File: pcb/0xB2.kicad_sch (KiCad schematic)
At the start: 37 parts, among them J1 USB_C_Receptacle_USB2.0, J2 Conn_01x12, J3 Conn_01x05, J4 Conn_01x12, SW1 SW_Push, SW2 SW_Push, U1 RP2040, U2 W25Q32JVZP, U3 AP2127K-3.3, Y1 Crystal_GND24

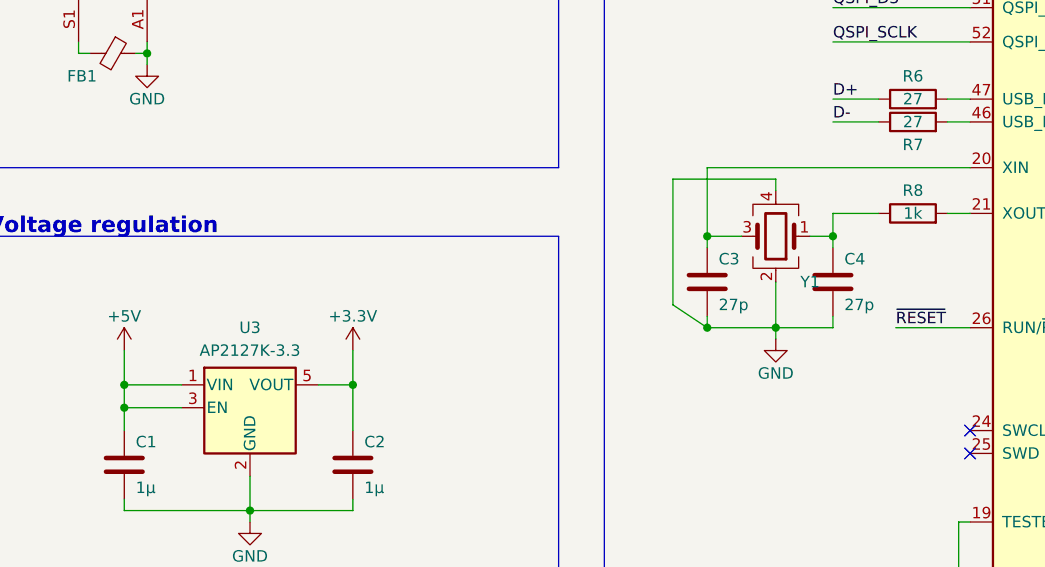
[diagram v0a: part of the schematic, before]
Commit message: Smaller crystal footprint > 2520
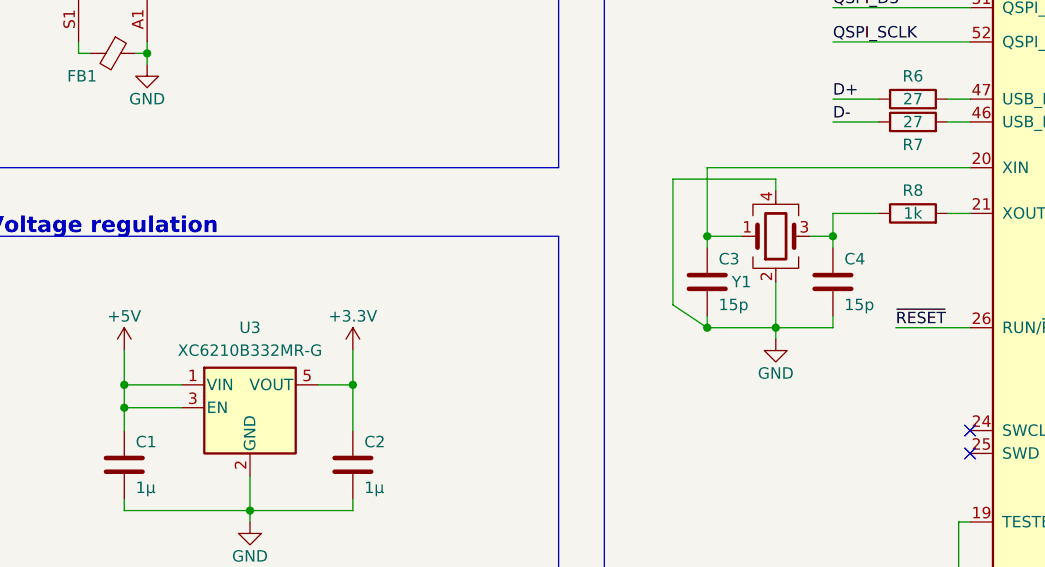
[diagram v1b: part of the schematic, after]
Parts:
- C3, C4: value 27p -> 15p; LCSC C1557 -> C1548
- U3: value AP2127K-3.3 -> XC6210B332MR-G; LCSC C47719 -> C82942; LCSC2 (none) -> C47719
- Y1: footprint Crystal:Crystal_SMD_3225-4Pin_3.2x2.5mm -> Crystal:Crystal_SMD_2520-4Pin_2.5x2.0mm; LCSC C97242 -> C2149204
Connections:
- net at C3.1, U1.20 (XIN): now also Y1.1; no longer Y1.3
- net at C4.1, R8.1: now also Y1.3; no longer Y1.1
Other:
- moved on the sheet: Y1
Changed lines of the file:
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@@
     (in_bom yes) (on_board yes)
     (property "Reference" "U3" (id 0) (at 46.99 106.68 0))
-    (property "Value" "AP2127K-3.3" (id 1) (at 46.99 109.22 0))
+    (property "Value" "XC6210B332MR-G" (id 1) (at 46.99 109.22 0))
     (property "Footprint" "Package_TO_SOT_SMD:SOT-23-5" (id 2) (at 46.99 107.315 0)
       (effects (font (size 1.27 1.27)) hide)
     )
-    (property "Datasheet" "https://www.diodes.com/assets/Datasheets/AP2127.pdf" (id 3) (at 46.99 113.03 0)
-      (effects (font (size 1.27 1.27)) hide)
-    )
-    (property "LCSC" "C47719" (id 4) (at 46.99 115.57 0)
+    (property "Datasheet" "" (id 3) (at 46.99 113.03 0)
+      (effects (font (size 1.27 1.27)) hide)
+    )
+    (property "LCSC" "C82942" (id 4) (at 46.99 115.57 0)
+      (effects (font (size 1.27 1.27)) hide)
+    )
+    (property "LCSC2" "C47719" (id 5) (at 46.99 115.57 0)
       (effects (font (size 1.27 1.27)) hide)
     )
@@
     (pin "2")
   )
-  (symbol (lib_id "Device:Crystal_GND24") (at 105.41 96.52 180) (unit 1)
-    (in_bom yes) (on_board yes)
-    (property "Reference" "Y1" (id 0) (at 109.22 101.6 0))
-    (property "Value" "Crystal_GND24" (id 1) (at 93.98 97.5614 0)
-      (effects (font (size 1.27 1.27)) hide)
-    )
-    (property "Footprint" "Crystal:Crystal_SMD_3225-4Pin_3.2x2.5mm" (id 2) (at 105.41 96.52 0)
+  (symbol (lib_id "Device:Crystal_GND24") (at 105.41 96.52 0) (mirror x) (unit 1)
+    (in_bom yes) (on_board yes)
+    (property "Reference" "Y1" (id 0) (at 101.6 101.6 0))
+    (property "Value" "Crystal_GND24" (id 1) (at 116.84 97.5614 0)
+      (effects (font (size 1.27 1.27)) hide)
+    )
+    (property "Footprint" "Crystal:Crystal_SMD_2520-4Pin_2.5x2.0mm" (id 2) (at 105.41 96.52 0)
       (effects (font (size 1.27 1.27)) hide)
     )
@@
       (effects (font (size 1.27 1.27)) hide)
     )
-    (property "LCSC" "C97242" (id 4) (at 105.41 96.52 0)
+    (property "LCSC" "C2149204" (id 4) (at 105.41 96.52 0)
       (effects (font (size 1.27 1.27)) hide)
     )
@@
       (effects (font (size 1.27 1.27)) (justify left))
     )
-    (property "Value" "27p" (id 1) (at 113.03 104.14 0)
+    (property "Value" "15p" (id 1) (at 113.03 104.14 0)
       (effects (font (size 1.27 1.27)) (justify left))
     )
@@
       (effects (font (size 1.27 1.27)) hide)
     )
-    (property "LCSC" "C1557" (id 4) (at 111.76 101.6 0)
+    (property "LCSC" "C1548" (id 4) (at 111.76 101.6 0)
       (effects (font (size 1.27 1.27)) hide)
     )
@@
       (effects (font (size 1.27 1.27)) (justify left))
     )
-    (property "Value" "27p" (id 1) (at 99.06 104.14 0)
+    (property "Value" "15p" (id 1) (at 99.06 104.14 0)
       (effects (font (size 1.27 1.27)) (justify left))
     )
@@
       (effects (font (size 1.27 1.27)) hide)
     )
-    (property "LCSC" "C1557" (id 4) (at 97.79 101.6 0)
+    (property "LCSC" "C1548" (id 4) (at 97.79 101.6 0)
       (effects (font (size 1.27 1.27)) hide)
     )
@@
     )
     (path "/c0b12aba-3c4f-4684-83d7-a5de2c7f97e9"
-      (reference "C3") (unit 1) (value "27p") (footprint "Capacitor_SMD:C_0402_1005Metric")
+      (reference "C3") (unit 1) (value "15p") (footprint "Capacitor_SMD:C_0402_1005Metric")
     )
     (path "/89a664f3-9470-4cc9-8840-97b4b2b29405"
-      (reference "C4") (unit 1) (value "27p") (footprint "Capacitor_SMD:C_0402_1005Metric")
+      (reference "C4") (unit 1) (value "15p") (footprint "Capacitor_SMD:C_0402_1005Metric")
     )
     (path "/3ed857fe-184a-43ae-8f36-82703b1b8349"
@@
     )
     (path "/33208a57-5054-4bad-b85f-35da7b25e7bb"
-      (reference "U3") (unit 1) (value "AP2127K-3.3") (footprint "Package_TO_SOT_SMD:SOT-23-5")
+      (reference "U3") (unit 1) (value "XC6210B332MR-G") (footprint "Package_TO_SOT_SMD:SOT-23-5")
     )
     (path "/4ba8f30d-b9de-4dee-94c4-5459f9c13a42"
-      (reference "Y1") (unit 1) (value "Crystal_GND24") (footprint "Crystal:Crystal_SMD_3225-4Pin_3.2x2.5mm")
-    )
-  )
+      (reference "Y1") (unit 1) (value "Crystal_GND24") (footprint "Crystal:Crystal_SMD_2520-4Pin_2.5x2.0mm")
+    )
+  )

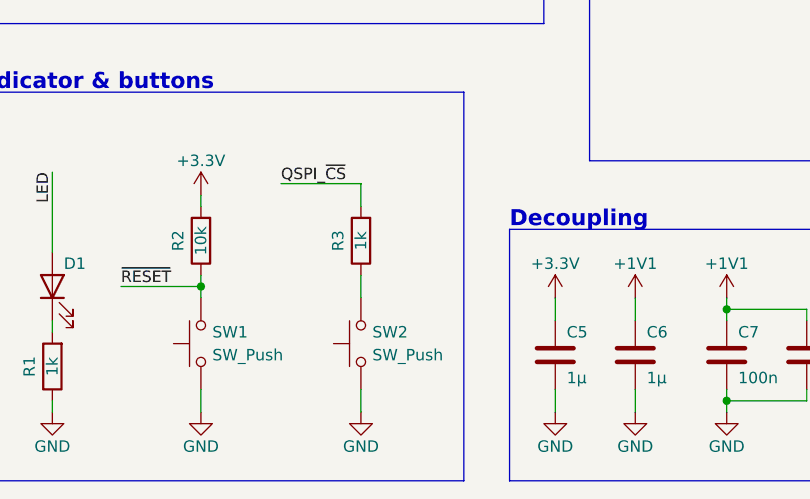
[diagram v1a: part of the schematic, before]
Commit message: Add BOOT pad on bottom layer
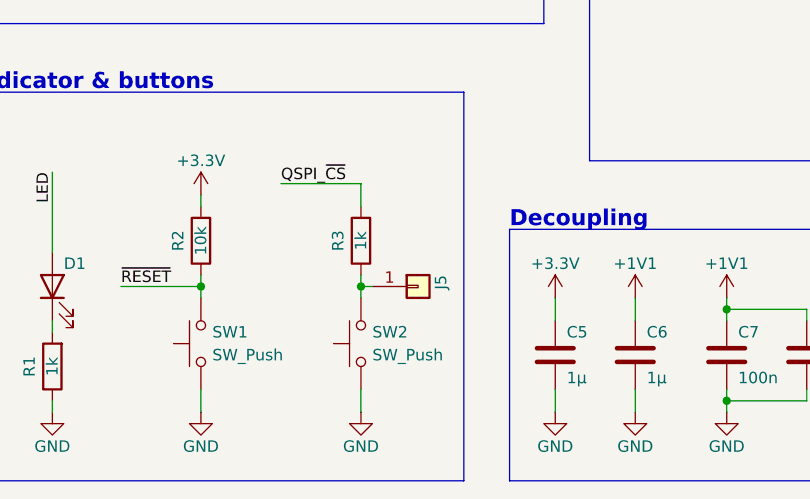
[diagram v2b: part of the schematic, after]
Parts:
- added J5: Conn_01x01, TestPoint:TestPoint_Pad_D1.0mm, symbol Connector_Generic:Conn_01x01
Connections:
- net at R3.1, SW2.2: now also J5.1 (Pin_1)
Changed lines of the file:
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@@
   (junction (at 71.12 44.45) (diameter 0) (color 0 0 0 0)
+  )
+  (junction (at 60.96 172.72) (diameter 0) (color 0 0 0 0)
   )
   (junction (at 130.81 185.42) (diameter 0) (color 0 0 0 0)
@@
     (stroke (width 0) (type default) (color 0 0 0 0))
   )
-  (wire (pts (xy 60.96 171.45) (xy 60.96 173.99))
+  (wire (pts (xy 60.96 171.45) (xy 60.96 172.72))
     (stroke (width 0) (type default) (color 0 0 0 0))
   )
@@
     (stroke (width 0) (type default) (color 0 0 0 0))
   )
+  (wire (pts (xy 60.96 172.72) (xy 60.96 173.99))
+    (stroke (width 0) (type default) (color 0 0 0 0))
+  )
   (wire (pts (xy 228.6 64.77) (xy 237.49 64.77))
     (stroke (width 0) (type default) (color 0 0 0 0))
@@
   )
   (wire (pts (xy 165.1 40.64) (xy 165.1 38.1))
+    (stroke (width 0) (type default) (color 0 0 0 0))
+  )
+  (wire (pts (xy 60.96 172.72) (xy 62.23 172.72))
     (stroke (width 0) (type default) (color 0 0 0 0))
   )
@@
     (pin "1")
   )
+  (symbol (lib_id "Connector_Generic:Conn_01x01") (at 67.31 172.72 0) (unit 1)
+    (in_bom yes) (on_board yes)
+    (property "Reference" "J5" (id 0) (at 69.85 171.45 90)
+      (effects (font (size 1.27 1.27)) (justify right))
+    )
+    (property "Value" "Conn_01x01" (id 1) (at 66.0401 175.26 90)
+      (effects (font (size 1.27 1.27)) (justify right) hide)
+    )
+    (property "Footprint" "TestPoint:TestPoint_Pad_D1.0mm" (id 2) (at 67.31 172.72 0)
+      (effects (font (size 1.27 1.27)) hide)
+    )
+    (property "Datasheet" "~" (id 3) (at 67.31 172.72 0)
+      (effects (font (size 1.27 1.27)) hide)
+    )
+    (pin "1")
+  )
   (symbol (lib_id "power:GND") (at 261.62 69.215 0) (unit 1)
     (in_bom yes) (on_board yes)
@@
       (reference "J4") (unit 1) (value "Conn_01x12") (footprint "0xLib_Connectors:PinHeader_1x12_P2.54mm")
     )
+    (path "/bc3a4b7a-f2c8-40bd-ac75-89d3e5ce5d5b"
+      (reference "J5") (unit 1) (value "Conn_01x01") (footprint "TestPoint:TestPoint_Pad_D1.0mm")
+    )
     (path "/81213cff-519c-4fcf-ae25-6fad0fc859bb"

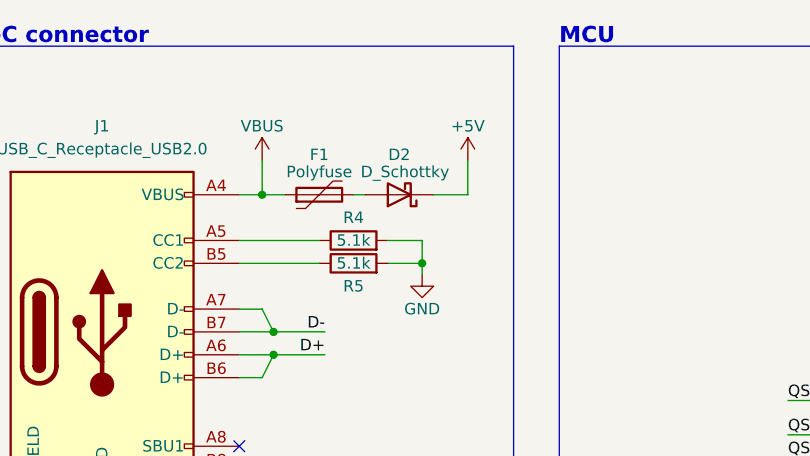
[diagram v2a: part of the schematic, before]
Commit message: New ref for D2
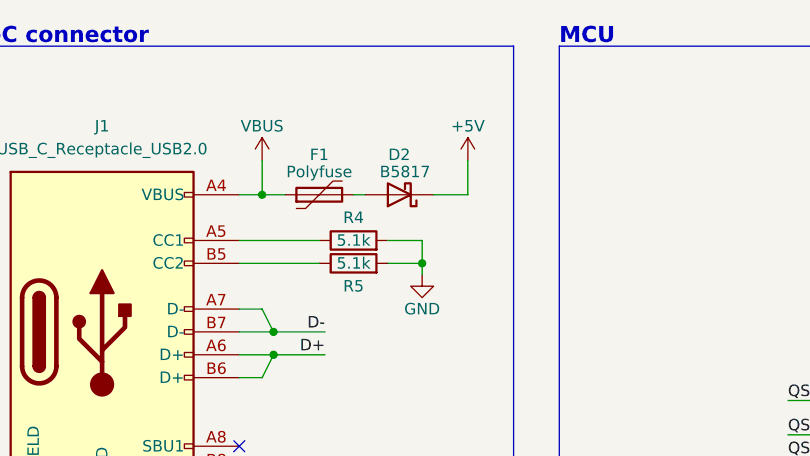
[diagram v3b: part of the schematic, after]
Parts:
- D2: value D_Schottky -> B5817; LCSC C22638 -> C123899
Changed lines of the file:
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@@
     (in_bom yes) (on_board yes)
     (property "Reference" "D2" (id 0) (at 68.58 32.385 0))
-    (property "Value" "D_Schottky" (id 1) (at 69.215 34.29 0))
+    (property "Value" "B5817" (id 1) (at 69.215 34.29 0))
     (property "Footprint" "Diode_SMD:D_SOD-323" (id 2) (at 68.58 36.83 0)
       (effects (font (size 1.27 1.27)) hide)
@@
       (effects (font (size 1.27 1.27)) hide)
     )
-    (property "LCSC" "C22638" (id 4) (at 68.58 36.83 0)
+    (property "LCSC" "C123899" (id 4) (at 68.58 36.83 0)
       (effects (font (size 1.27 1.27)) hide)
     )
@@
     )
     (path "/f97de4cd-aa39-42c5-ace3-9184b5a62b38"
-      (reference "D2") (unit 1) (value "D_Schottky") (footprint "Diode_SMD:D_SOD-323")
+      (reference "D2") (unit 1) (value "B5817") (footprint "Diode_SMD:D_SOD-323")
     )
     (path "/ce9365fe-085a-4731-86d8-fc3e6b16f716"

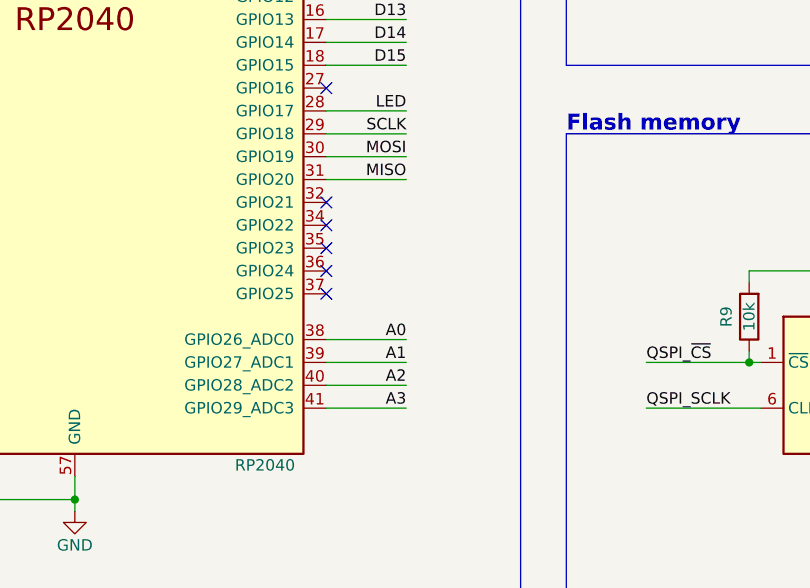
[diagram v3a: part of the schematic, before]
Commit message: Add USB VBUS detect on GPIO 25
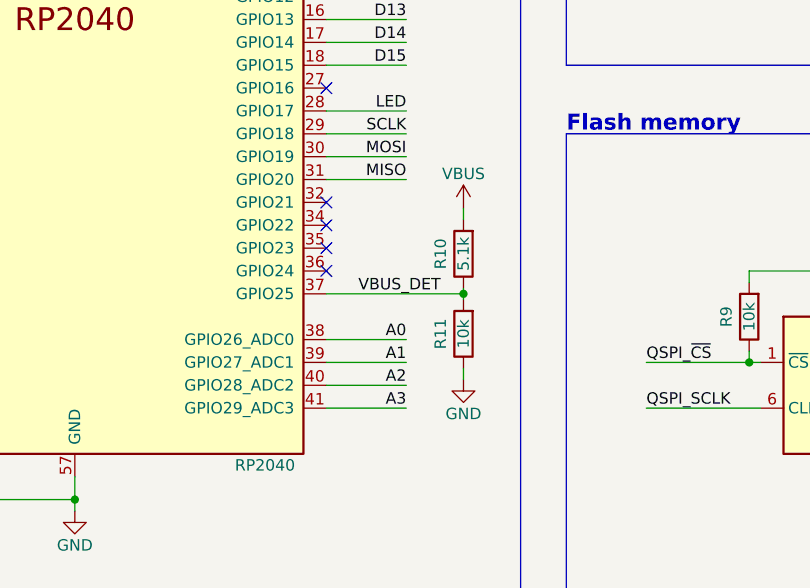
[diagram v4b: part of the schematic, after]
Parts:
- added R10: 5.1k, Resistor_SMD:R_0402_1005Metric, symbol Device:R
- added R11: 10k, Resistor_SMD:R_0402_1005Metric, symbol Device:R
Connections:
- net GND: now also R11.1
- net VBUS: now also R10.2
- net VBUS_DET: now reaches U1.37 (GPIO25)
- net VBUS_DET: now also R10.1, R11.2
- no-connect marks 10 -> 9
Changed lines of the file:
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@@
   (junction (at 35.56 76.2) (diameter 0) (color 0 0 0 0)
   )
+  (junction (at 198.12 121.92) (diameter 0) (color 0 0 0 0)
+  )
   (junction (at 231.14 46.99) (diameter 0) (color 0 0 0 0)
   )
@@
   )
   (no_connect (at 182.88 119.38))
-  (no_connect (at 182.88 121.92))
   (no_connect (at 182.88 116.84))
   (no_connect (at 182.88 111.76))
@@
     (stroke (width 0) (type default) (color 0 0 0 0))
   )
+  (wire (pts (xy 198.12 130.175) (xy 198.12 131.445))
+    (stroke (width 0) (type default) (color 0 0 0 0))
+  )
   (wire (pts (xy 143.51 38.1) (xy 143.51 40.64))
     (stroke (width 0) (type default) (color 0 0 0 0))
@@
     (stroke (width 0) (type default) (color 0 0 0 0))
   )
+  (wire (pts (xy 198.12 121.92) (xy 198.12 122.555))
+    (stroke (width 0) (type default) (color 0 0 0 0))
+  )
   (wire (pts (xy 139.7 184.15) (xy 139.7 185.42))
     (stroke (width 0) (type default) (color 0 0 0 0))
@@
     (stroke (width 0) (type default) (color 0 0 0 0))
   )
+  (wire (pts (xy 182.88 121.92) (xy 198.12 121.92))
+    (stroke (width 0) (type default) (color 0 0 0 0))
+  )
   (wire (pts (xy 243.84 119.38) (xy 243.84 121.92))
     (stroke (width 0) (type default) (color 0 0 0 0))
@@
     (stroke (width 0) (type default) (color 0 0 0 0))
   )
+  (wire (pts (xy 198.12 112.395) (xy 198.12 113.665))
+    (stroke (width 0) (type default) (color 0 0 0 0))
+  )
   (wire (pts (xy 124.46 83.82) (xy 127 83.82))
     (stroke (width 0) (type default) (color 0 0 0 0))
@@
   )
   (wire (pts (xy 162.56 38.1) (xy 162.56 40.64))
+    (stroke (width 0) (type default) (color 0 0 0 0))
+  )
+  (wire (pts (xy 198.12 121.285) (xy 198.12 121.92))
     (stroke (width 0) (type default) (color 0 0 0 0))
   )
@@
   )
   (label "D0" (at 237.49 39.37 180)
+    (effects (font (size 1.27 1.27)) (justify right bottom))
+  )
+  (label "VBUS_DET" (at 195.58 121.92 180)
     (effects (font (size 1.27 1.27)) (justify right bottom))
   )
@@
     (pin "2")
   )
+  (symbol (lib_id "Device:R") (at 198.12 117.475 180) (unit 1)
+    (in_bom yes) (on_board yes)
+    (property "Reference" "R10" (id 0) (at 195.58 117.475 90))
+    (property "Value" "5.1k" (id 1) (at 198.12 117.475 90))
+    (property "Footprint" "Resistor_SMD:R_0402_1005Metric" (id 2) (at 199.898 117.475 90)
+      (effects (font (size 1.27 1.27)) hide)
+    )
+    (property "Datasheet" "~" (id 3) (at 198.12 117.475 0)
+      (effects (font (size 1.27 1.27)) hide)
+    )
+    (property "LCSC" "C25905" (id 4) (at 198.12 117.475 0)
+      (effects (font (size 1.27 1.27)) hide)
+    )
+    (pin "1")
+    (pin "2")
+  )
   (symbol (lib_id "Device:C") (at 157.48 180.34 0) (unit 1)
     (in_bom yes) (on_board yes)
@@
     )
     (pin "1")
+  )
+  (symbol (lib_id "Device:R") (at 198.12 126.365 180) (unit 1)
+    (in_bom yes) (on_board yes)
+    (property "Reference" "R11" (id 0) (at 195.58 126.365 90))
+    (property "Value" "10k" (id 1) (at 198.12 126.365 90))
+    (property "Footprint" "Resistor_SMD:R_0402_1005Metric" (id 2) (at 199.898 126.365 90)
+      (effects (font (size 1.27 1.27)) hide)
+    )
+    (property "Datasheet" "~" (id 3) (at 198.12 126.365 0)
+      (effects (font (size 1.27 1.27)) hide)
+    )
+    (property "LCSC" "C25744" (id 4) (at 198.12 126.365 0)
+      (effects (font (size 1.27 1.27)) hide)
+    )
+    (pin "1")
+    (pin "2")
   )
   (symbol (lib_id "Device:LED") (at 26.67 172.72 90) (unit 1)
@@
     (pin "1")
   )
+  (symbol (lib_id "power:GND") (at 198.12 131.445 0) (unit 1)
+    (in_bom yes) (on_board yes)
+    (property "Reference" "#PWR0101" (id 0) (at 198.12 137.795 0)
+      (effects (font (size 1.27 1.27)) hide)
+    )
+    (property "Value" "GND" (id 1) (at 198.12 135.255 0))
+    (property "Footprint" "" (id 2) (at 198.12 131.445 0)
+      (effects (font (size 1.27 1.27)) hide)
+    )
+    (property "Datasheet" "" (id 3) (at 198.12 131.445 0)
+      (effects (font (size 1.27 1.27)) hide)
+    )
+    (pin "1")
+  )
   (symbol (lib_id "power:+3.3V") (at 134.62 36.83 0) (unit 1)
     (in_bom yes) (on_board yes)
@@
     (pin "2")
   )
+  (symbol (lib_id "power:VBUS") (at 198.12 112.395 0) (unit 1)
+    (in_bom yes) (on_board yes)
+    (property "Reference" "#PWR0102" (id 0) (at 198.12 116.205 0)
+      (effects (font (size 1.27 1.27)) hide)
+    )
+    (property "Value" "VBUS" (id 1) (at 198.12 108.585 0))
+    (property "Footprint" "" (id 2) (at 198.12 112.395 0)
+      (effects (font (size 1.27 1.27)) hide)
+    )
+    (property "Datasheet" "" (id 3) (at 198.12 112.395 0)
+      (effects (font (size 1.27 1.27)) hide)
+    )
+    (pin "1")
+  )
   (sheet_instances
     (path "/" (page "1"))
@@
       (reference "#PWR031") (unit 1) (value "VBUS") (footprint "")
     )
+    (path "/da1644f7-6b59-4f28-b4bd-963f2f055bce"
+      (reference "#PWR0101") (unit 1) (value "GND") (footprint "")
+    )
+    (path "/f9f9d52c-c3cf-4935-8d1b-0924649d81e5"
+      (reference "#PWR0102") (unit 1) (value "VBUS") (footprint "")
+    )
     (path "/4a21e78b-0ab0-4b88-8132-9b174e045719"
       (reference "C1") (unit 1) (value "1µ") (footprint "Capacitor_SMD:C_0603_1608Metric")
@@
       (reference "R9") (unit 1) (value "10k") (footprint "Resistor_SMD:R_0402_1005Metric")
     )
+    (path "/240ef12d-5727-43f1-8ff0-84f44af2df0d"
+      (reference "R10") (unit 1) (value "5.1k") (footprint "Resistor_SMD:R_0402_1005Metric")
+    )
+    (path "/5853345e-306a-41fe-bca6-c90c415bf536"
+      (reference "R11") (unit 1) (value "10k") (footprint "Resistor_SMD:R_0402_1005Metric")
+    )
     (path "/c30a3276-ac5c-4a68-880e-26478e1b53e4"
